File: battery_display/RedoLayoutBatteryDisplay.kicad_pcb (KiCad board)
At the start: 2 copper layers, 97 x 60 mm, 27 parts, among them J1 FH34SRJ-24S-0.5SH_99_, J2 Screw_Terminal_2x2.54, Q2 ZXM61N03F, SW1 Button

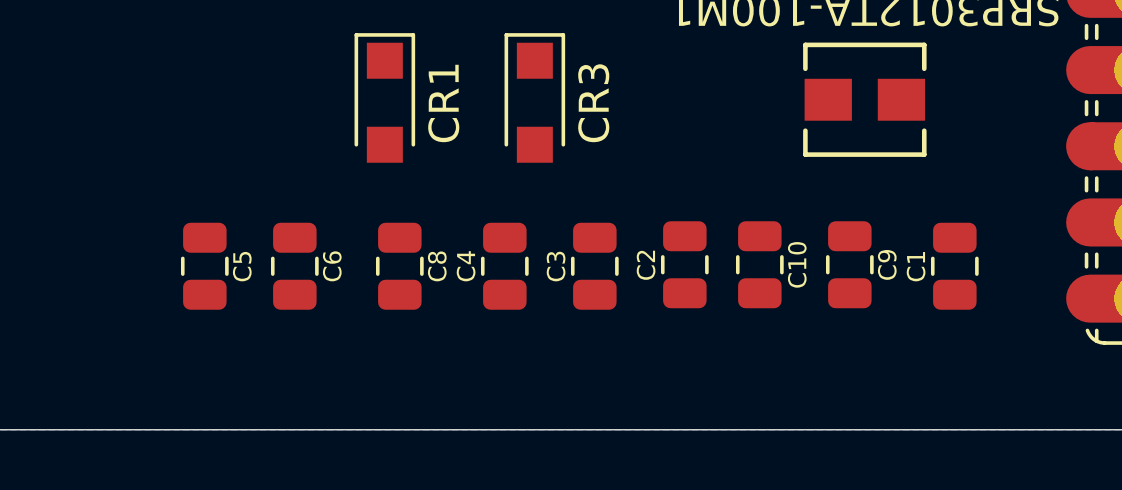
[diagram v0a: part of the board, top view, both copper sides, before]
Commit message: fixed some errors
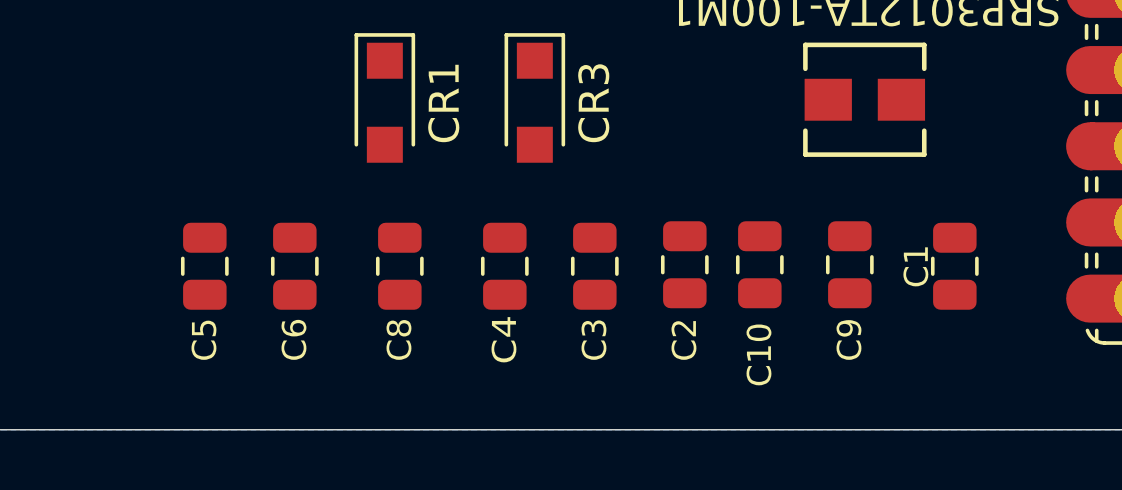
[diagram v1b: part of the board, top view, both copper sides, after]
